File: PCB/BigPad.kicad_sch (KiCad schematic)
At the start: 27 parts, among them SW1 RotaryEncoder_Switch, SW2 RotaryEncoder_Switch

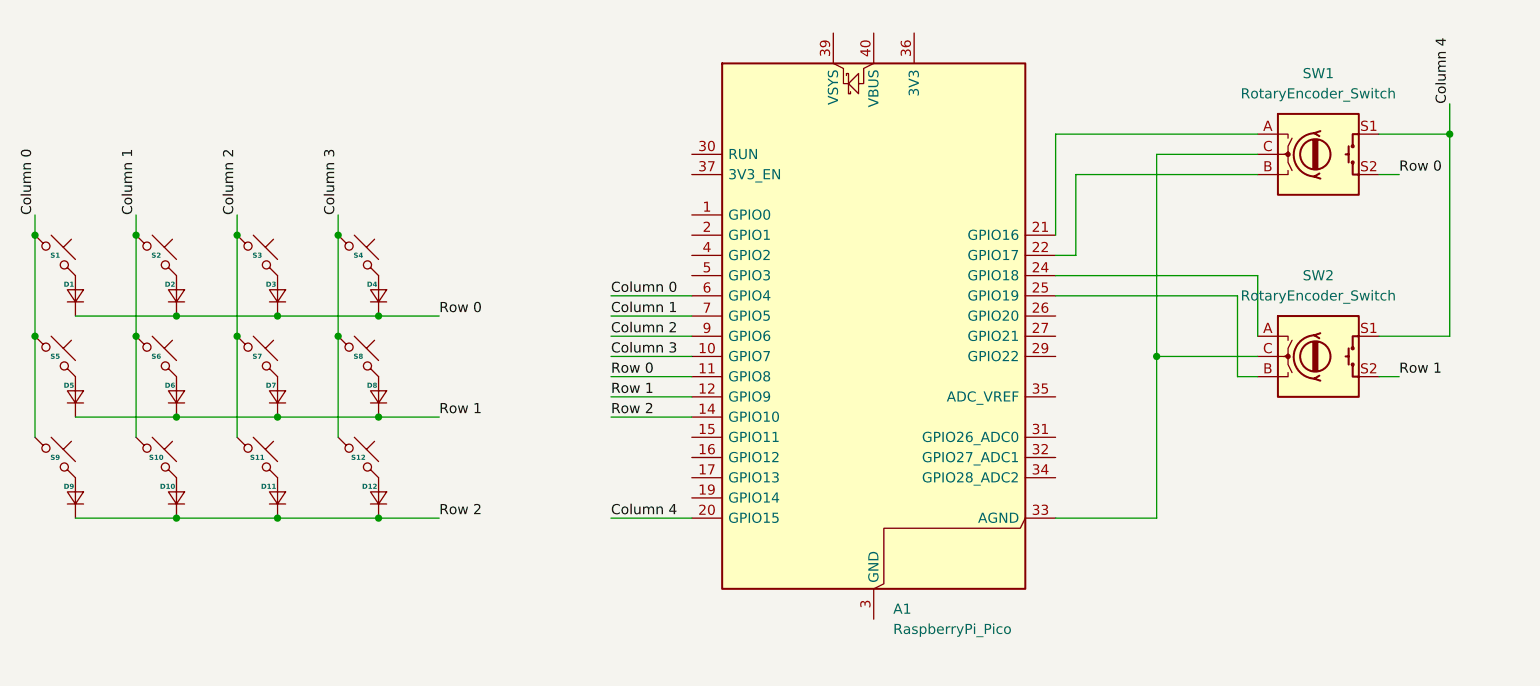
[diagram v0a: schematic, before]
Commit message: Updated rotary encoder wiring in schematic
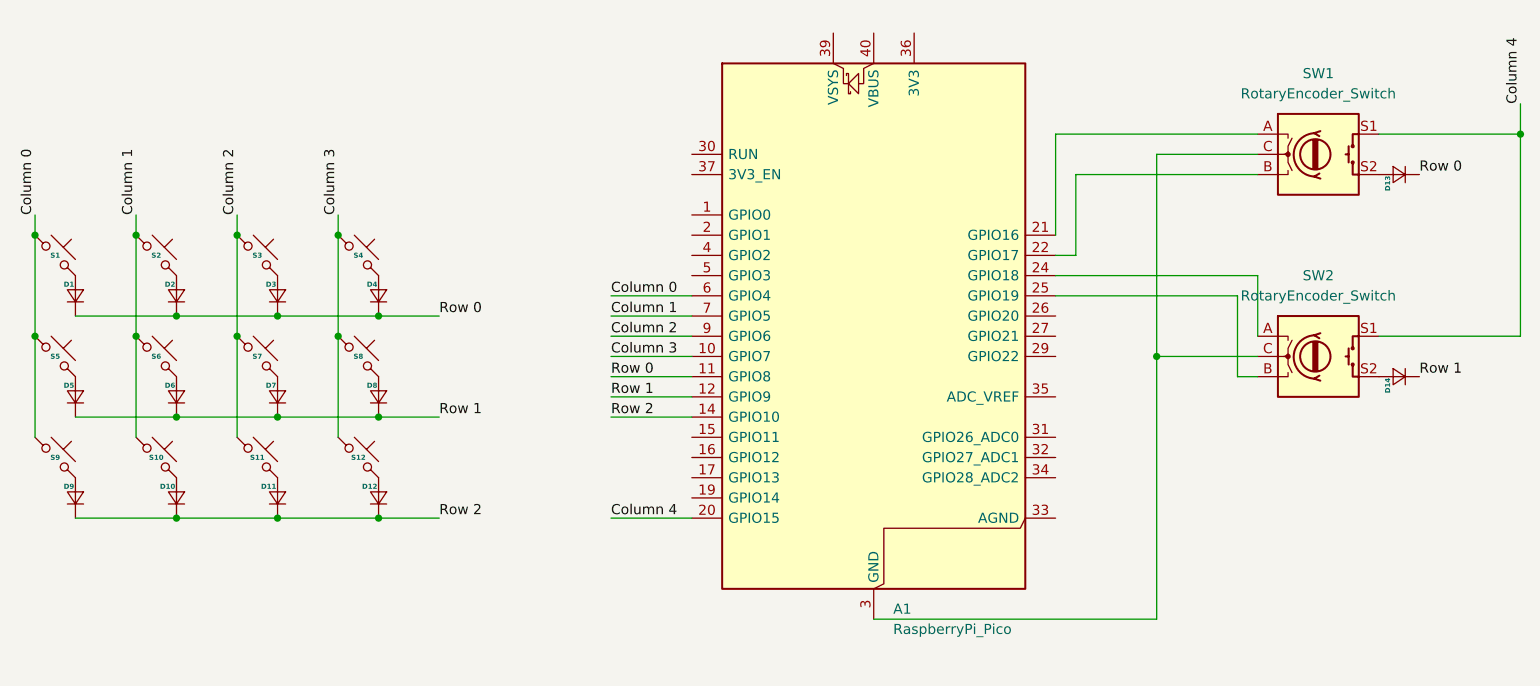
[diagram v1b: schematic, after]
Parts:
- added D13, D14: (no value), ScottoKeebs_Components:Diode_DO-35, symbol ScottoKeebs:Placeholder_Diode
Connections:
- net Row 0: now also D13.1 (K); no longer SW1.S2
- net Row 1: now also D14.1 (K); no longer SW2.S2
- net at SW1.C, SW2.C: now also A1.13 (GND), A1.18 (GND), A1.23 (GND), A1.28 (GND), A1.3 (GND), A1.38 (GND), A1.8 (GND); no longer A1.33 (AGND)
- new net: D14.2 (A), SW2.S2
- new net: D13.2 (A), SW1.S2
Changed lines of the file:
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@@
-	)
-	(junction
-		(at 201.93 54.61)
-		(diameter 0)
-		(color 0 0 0 0)
 	)
 	(junction
@@
 	)
 	(junction
+		(at 210.82 54.61)
+		(diameter 0)
+		(color 0 0 0 0)
+	)
+	(junction
 		(at 67.31 102.87)
 		(diameter 0)
@@
 	(wire
 		(pts
-			(xy 201.93 54.61) (xy 193.04 54.61)
+			(xy 193.04 54.61) (xy 210.82 54.61)
 		)
 		(stroke
@@
 	(wire
 		(pts
-			(xy 152.4 102.87) (xy 165.1 102.87)
-		)
-		(stroke
-			(width 0)
-			(type default)
-		)
-	)
-	(wire
-		(pts
 			(xy 96.52 87.63) (xy 106.68 87.63)
 		)
@@
 	(wire
 		(pts
-			(xy 193.04 80.01) (xy 201.93 80.01)
+			(xy 193.04 80.01) (xy 210.82 80.01)
 		)
 		(stroke
@@
 	(wire
 		(pts
-			(xy 195.58 59.69) (xy 193.04 59.69)
-		)
-		(stroke
-			(width 0)
-			(type default)
-		)
-	)
-	(wire
-		(pts
 			(xy 177.8 57.15) (xy 165.1 57.15)
 		)
@@
 	(wire
 		(pts
-			(xy 165.1 102.87) (xy 165.1 82.55)
-		)
-		(stroke
-			(width 0)
-			(type default)
-		)
-	)
-	(wire
-		(pts
-			(xy 201.93 54.61) (xy 201.93 80.01)
+			(xy 165.1 82.55) (xy 165.1 115.57)
+		)
+		(stroke
+			(width 0)
+			(type default)
+		)
+	)
+	(wire
+		(pts
+			(xy 210.82 54.61) (xy 210.82 80.01)
 		)
 		(stroke
@@
 	(wire
 		(pts
+			(xy 165.1 115.57) (xy 129.54 115.57)
+		)
+		(stroke
+			(width 0)
+			(type default)
+		)
+	)
+	(wire
+		(pts
 			(xy 154.94 59.69) (xy 177.8 59.69)
 		)
@@
 	(wire
 		(pts
-			(xy 195.58 85.09) (xy 193.04 85.09)
-		)
-		(stroke
-			(width 0)
-			(type default)
-		)
-	)
-	(wire
-		(pts
 			(xy 74.93 90.17) (xy 67.31 90.17)
 		)
@@
 	(wire
 		(pts
-			(xy 201.93 50.8) (xy 201.93 54.61)
+			(xy 210.82 50.8) (xy 210.82 54.61)
 		)
 		(stroke
@@
 	)
 	(label "Row 0"
-		(at 195.58 59.69 0)
-		(effects
-			(font
-				(size 1.27 1.27)
-			)
-			(justify left bottom)
-		)
-	)
-	(label "Row 0"
 		(at 74.93 77.47 0)
 		(effects
@@
 	)
 	(label "Column 4"
-		(at 201.93 50.8 90)
+		(at 210.82 50.8 90)
 		(effects
 			(font
@@
 		)
 	)
+	(label "Row 0"
+		(at 198.12 59.69 0)
+		(effects
+			(font
+				(size 1.27 1.27)
+			)
+			(justify left bottom)
+		)
+	)
 	(label "Column 2"
 		(at 49.53 64.77 90)
@@
 		)
 	)
+	(label "Row 1"
+		(at 198.12 85.09 0)
+		(effects
+			(font
+				(size 1.27 1.27)
+			)
+			(justify left bottom)
+		)
+	)
 	(label "Column 1"
 		(at 96.52 77.47 0)
@@
 	(label "Column 4"
 		(at 96.52 102.87 0)
-		(effects
-			(font
-				(size 1.27 1.27)
-			)
-			(justify left bottom)
-		)
-	)
-	(label "Row 1"
-		(at 195.58 85.09 0)
 		(effects
 			(font
@@
 	)
 	(symbol
+		(lib_id "ScottoKeebs:Placeholder_Diode")
+		(at 195.58 85.09 90)
+		(unit 1)
+		(body_style 1)
+		(exclude_from_sim no)
+		(in_bom yes)
+		(on_board yes)
+		(in_pos_files yes)
+		(dnp no)
+		(fields_autoplaced yes)
+		(property "Reference" "D14"
+			(at 194.514 85.24 0)
+			(show_name no)
+			(do_not_autoplace yes)
+			(effects
+				(font
+					(size 0.635 0.635)
+					(thickness 0.127)
+					(bold yes)
+				)
+				(justify right bottom)
+			)
+		)
+		(property "Value" ""
+			(at 195.58 82.55 90)
+			(show_name no)
+			(do_not_autoplace no)
+			(effects
+				(font
+					(size 1.27 1.27)
+				)
+			)
+		)
+		(property "Footprint" "ScottoKeebs_Components:Diode_DO-35"
+			(at 195.58 85.09 90)
+			(hide yes)
+			(show_name no)
+			(do_not_autoplace no)
+			(effects
+				(font
+					(size 1.27 1.27)
+				)
+			)
+		)
+		(property "Datasheet" ""
+			(at 195.58 85.09 90)
+			(hide yes)
+			(show_name no)
+			(do_not_autoplace no)
+			(effects
+				(font
+					(size 1.27 1.27)
+				)
+			)
+		)
+		(property "Description" ""
+			(at 195.58 81.28 90)
+			(hide yes)
+			(show_name no)
+			(do_not_autoplace no)
+			(effects
+				(font
+					(size 1.27 1.27)
+				)
+			)
+		)
+		(pin "1"
+		)
+		(pin "2"
+		)
+		(instances
+			(project "BigPad"
+				(path "/57af516c-98c7-406a-8dd4-07f33deb6b10"
+					(reference "D14")
+					(unit 1)
+				)
+			)
+		)
+	)
+	(symbol
 		(lib_id "ScottoKeebs:Placeholder_Keyswitch")
 		(at 39.37 82.55 0)
@@
 					(unit 1)
 				)
+			)
+		)
+	)
+	(symbol
+		(lib_id "ScottoKeebs:Placeholder_Diode")
+		(at 195.58 59.69 90)
+		(unit 1)
+		(body_style 1)
+		(exclude_from_sim no)
+		(in_bom yes)
+		(on_board yes)
+		(in_pos_files yes)
+		(dnp no)
+		(fields_autoplaced yes)
+		(property "Reference" "D13"
+			(at 194.514 59.84 0)
+			(show_name no)
+			(do_not_autoplace yes)
+			(effects
+				(font
+					(size 0.635 0.635)
+					(thickness 0.127)
+					(bold yes)
+				)
+				(justify right bottom)
+			)
+		)
+		(property "Value" ""
+			(at 195.58 57.15 90)
+			(show_name no)
+			(do_not_autoplace no)
+			(effects
+				(font
+					(size 1.27 1.27)
+				)
+			)
+		)
+		(property "Footprint" "ScottoKeebs_Components:Diode_DO-35"
+			(at 195.58 59.69 90)
+			(hide yes)
+			(show_name no)
+			(do_not_autoplace no)
+			(effects
+				(font
+					(size 1.27 1.27)
+				)
+			)
+		)
+		(property "Datasheet" ""
+			(at 195.58 59.69 90)
+			(hide yes)
+			(show_name no)
+			(do_not_autoplace no)
+			(effects
+				(font
+					(size 1.27 1.27)
+				)
+			)
+		)
+		(property "Description" ""
+			(at 195.58 55.88 90)
+			(hide yes)
+			(show_name no)
+			(do_not_autoplace no)
+			(effects
+				(font
+					(size 1.27 1.27)
+				)
+			)
+		)
+		(pin "1"
+		)
+		(pin "2"
+		)
+		(instances
+			(project "BigPad"
+				(path "/57af516c-98c7-406a-8dd4-07f33deb6b10"
+					(reference "D13")
+					(unit 1)
+				)

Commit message: completed rotary encoders in PCB design
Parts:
- A1: footprint Module:RaspberryPi_Pico_Common_SMD -> Module:RaspberryPi_Pico_Common_THT
- SW1, SW2: footprint (none) -> Rotary_Encoder:RotaryEncoder_Alps_EC11E-Switch_Vertical_H20mm_MountingHoles
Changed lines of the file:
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@@
 			)
 		)
-		(property "Footprint" ""
+		(property "Footprint" "Rotary_Encoder:RotaryEncoder_Alps_EC11E-Switch_Vertical_H20mm_MountingHoles"
 			(at 181.61 53.086 0)
 			(hide yes)
@@
 			)
 		)
-		(property "Footprint" "Module:RaspberryPi_Pico_Common_SMD"
+		(property "Footprint" "Module:RaspberryPi_Pico_Common_THT"
 			(at 129.54 127 0)
 			(hide yes)
@@
 			)
 		)
-		(property "Footprint" ""
+		(property "Footprint" "Rotary_Encoder:RotaryEncoder_Alps_EC11E-Switch_Vertical_H20mm_MountingHoles"
 			(at 181.61 78.486 0)
 			(hide yes)

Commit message: fixed several wiring issues
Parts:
- D1, D10, D11, D12, D13, D14, D2, D3, D4, D5, D6, D7, D8, D9: footprint ScottoKeebs_Components:Diode_DO-35 -> Diode_SMD:D_SOD-123
- S1, S10, S11, S12, S2, S3, S4, S5, S6, S7, S8, S9: footprint ScottoKeebs_MX:MX_PCB_1.00u -> PCM_Switch_Keyboard_Hotswap_Kailh:SW_Hotswap_Kailh_MX_Plated_1.00u
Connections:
- net GND: now reaches A1.13 (GND), A1.18 (GND), A1.23 (GND), A1.28 (GND), A1.3 (GND), A1.38 (GND), A1.8 (GND), SW1.C, SW2.C
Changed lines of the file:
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@@
 	)
 	(junction
-		(at 165.1 82.55)
-		(diameter 0)
-		(color 0 0 0 0)
-	)
-	(junction
 		(at 41.91 102.87)
 		(diameter 0)
@@
 	)
 	(junction
+		(at 165.1 82.55)
+		(diameter 0)
+		(color 0 0 0 0)
+	)
+	(junction
 		(at 67.31 77.47)
 		(diameter 0)
@@
 	(wire
 		(pts
+			(xy 165.1 86.36) (xy 165.1 82.55)
+		)
+		(stroke
+			(width 0)
+			(type default)
+		)
+	)
+	(wire
+		(pts
 			(xy 74.93 77.47) (xy 67.31 77.47)
 		)
@@
 	(wire
 		(pts
-			(xy 165.1 82.55) (xy 165.1 115.57)
-		)
-		(stroke
-			(width 0)
-			(type default)
-		)
-	)
-	(wire
-		(pts
 			(xy 210.82 54.61) (xy 210.82 80.01)
 		)
@@
 	(wire
 		(pts
-			(xy 165.1 115.57) (xy 129.54 115.57)
-		)
-		(stroke
-			(width 0)
-			(type default)
-		)
-	)
-	(wire
-		(pts
 			(xy 154.94 59.69) (xy 177.8 59.69)
 		)
@@
 	)
 	(symbol
+		(lib_id "power:GND")
+		(at 129.54 115.57 0)
+		(unit 1)
+		(body_style 1)
+		(exclude_from_sim no)
+		(in_bom yes)
+		(on_board yes)
+		(in_pos_files yes)
+		(dnp no)
+		(fields_autoplaced yes)
+		(property "Reference" "#PWR01"
+			(at 129.54 121.92 0)
+			(hide yes)
+			(show_name no)
+			(do_not_autoplace no)
+			(effects
+				(font
+					(size 1.27 1.27)
+				)
+			)
+		)
+		(property "Value" "GND"
+			(at 129.54 120.65 0)
+			(show_name no)
+			(do_not_autoplace no)
+			(effects
+				(font
+					(size 1.27 1.27)
+				)
+			)
+		)
+		(property "Footprint" ""
+			(at 129.54 115.57 0)
+			(hide yes)
+			(show_name no)
+			(do_not_autoplace no)
+			(effects
+				(font
+					(size 1.27 1.27)
+				)
+			)
+		)
+		(property "Datasheet" ""
+			(at 129.54 115.57 0)
+			(hide yes)
+			(show_name no)
+			(do_not_autoplace no)
+			(effects
+				(font
+					(size 1.27 1.27)
+				)
+			)
+		)
+		(property "Description" "Power symbol creates a global label with name \"GND\" , ground"
+			(at 129.54 115.57 0)
+			(hide yes)
+			(show_name no)
+			(do_not_autoplace no)
+			(effects
+				(font
+					(size 1.27 1.27)
+				)
+			)
+		)
+		(pin "1"
+		)
+		(instances
+			(project "BigPad"
+				(path "/57af516c-98c7-406a-8dd4-07f33deb6b10"
+					(reference "#PWR01")
+					(unit 1)
+				)
+			)
+		)
+	)
+	(symbol
 		(lib_id "ScottoKeebs:Placeholder_Keyswitch")
 		(at 39.37 69.85 0)
@@
 			)
 		)
-		(property "Footprint" "ScottoKeebs_MX:MX_PCB_1.00u"
+		(property "Footprint" "PCM_Switch_Keyboard_Hotswap_Kailh:SW_Hotswap_Kailh_MX_Plated_1.00u"
 			(at 39.37 69.85 0)
 			(hide yes)
@@
 			)
 		)
-		(property "Footprint" "ScottoKeebs_Components:Diode_DO-35"
+		(property "Footprint" "Diode_SMD:D_SOD-123"
 			(at 195.58 85.09 90)
 			(hide yes)
@@
 			)
 		)
-		(property "Footprint" "ScottoKeebs_MX:MX_PCB_1.00u"
+		(property "Footprint" "PCM_Switch_Keyboard_Hotswap_Kailh:SW_Hotswap_Kailh_MX_Plated_1.00u"
 			(at 39.37 82.55 0)
 			(hide yes)
@@
 			)
 		)
-		(property "Footprint" "ScottoKeebs_Components:Diode_DO-35"
+		(property "Footprint" "Diode_SMD:D_SOD-123"
 			(at 54.61 87.63 90)
 			(hide yes)
@@
 			)
 		)
-		(property "Footprint" "ScottoKeebs_Components:Diode_DO-35"
+		(property "Footprint" "Diode_SMD:D_SOD-123"
 			(at 195.58 59.69 90)
 			(hide yes)
@@
 			)
 		)
-		(property "Footprint" "ScottoKeebs_Components:Diode_DO-35"
+		(property "Footprint" "Diode_SMD:D_SOD-123"
 			(at 29.21 87.63 90)
 			(hide yes)
@@
 			)
 		)
-		(property "Footprint" "ScottoKeebs_Components:Diode_DO-35"
+		(property "Footprint" "Diode_SMD:D_SOD-123"
 			(at 67.31 100.33 90)
 			(hide yes)
@@
 			)
 		)
-		(property "Footprint" "ScottoKeebs_Components:Diode_DO-35"
+		(property "Footprint" "Diode_SMD:D_SOD-123"
 			(at 67.31 87.63 90)
 			(hide yes)
@@
 			)
 		)
-		(property "Footprint" "ScottoKeebs_Components:Diode_DO-35"
+		(property "Footprint" "Diode_SMD:D_SOD-123"
 			(at 67.31 74.93 90)
 			(hide yes)
@@
 			)
 		)
-		(property "Footprint" "ScottoKeebs_Components:Diode_DO-35"
+		(property "Footprint" "Diode_SMD:D_SOD-123"
 			(at 29.21 74.93 90)
 			(hide yes)
@@
 	)
 	(symbol
+		(lib_id "power:GND")
+		(at 165.1 86.36 0)
+		(unit 1)
+		(body_style 1)
+		(exclude_from_sim no)
+		(in_bom yes)
+		(on_board yes)
+		(in_pos_files yes)
+		(dnp no)
+		(fields_autoplaced yes)
+		(property "Reference" "#PWR02"
+			(at 165.1 92.71 0)
+			(hide yes)
+			(show_name no)
+			(do_not_autoplace no)
+			(effects
+				(font
+					(size 1.27 1.27)
+				)
+			)
+		)
+		(property "Value" "GND"
+			(at 165.1 91.44 0)
+			(show_name no)
+			(do_not_autoplace no)
+			(effects
+				(font
+					(size 1.27 1.27)
+				)
+			)
+		)
+		(property "Footprint" ""
+			(at 165.1 86.36 0)
+			(hide yes)
+			(show_name no)
+			(do_not_autoplace no)
+			(effects
+				(font
+					(size 1.27 1.27)
+				)
+			)
+		)
+		(property "Datasheet" ""
+			(at 165.1 86.36 0)
+			(hide yes)
+			(show_name no)
+			(do_not_autoplace no)
+			(effects
+				(font
+					(size 1.27 1.27)
+				)
+			)
+		)
+		(property "Description" "Power symbol creates a global label with name \"GND\" , ground"
+			(at 165.1 86.36 0)
+			(hide yes)
+			(show_name no)
+			(do_not_autoplace no)
+			(effects
+				(font
+					(size 1.27 1.27)
+				)
+			)
+		)
+		(pin "1"
+		)
+		(instances
+			(project "BigPad"
+				(path "/57af516c-98c7-406a-8dd4-07f33deb6b10"
+					(reference "#PWR02")
+					(unit 1)
+				)
+			)
+		)
+	)
+	(symbol
 		(lib_id "ScottoKeebs:Placeholder_Keyswitch")
 		(at 64.77 82.55 0)
@@
 			)
 		)
-		(property "Footprint" "ScottoKeebs_MX:MX_PCB_1.00u"
+		(property "Footprint" "PCM_Switch_Keyboard_Hotswap_Kailh:SW_Hotswap_Kailh_MX_Plated_1.00u"
 			(at 64.77 82.55 0)
 			(hide yes)
@@
 			)
 		)
-		(property "Footprint" "ScottoKeebs_Components:Diode_DO-35"
+		(property "Footprint" "Diode_SMD:D_SOD-123"
 			(at 41.91 74.93 90)
 			(hide yes)
@@
 			)
 		)
-		(property "Footprint" "ScottoKeebs_MX:MX_PCB_1.00u"
+		(property "Footprint" "PCM_Switch_Keyboard_Hotswap_Kailh:SW_Hotswap_Kailh_MX_Plated_1.00u"
 			(at 26.67 82.55 0)
 			(hide yes)
@@
 			)
 		)
-		(property "Footprint" "ScottoKeebs_MX:MX_PCB_1.00u"
+		(property "Footprint" "PCM_Switch_Keyboard_Hotswap_Kailh:SW_Hotswap_Kailh_MX_Plated_1.00u"
 			(at 52.07 95.25 0)
 			(hide yes)
@@
 			)
 		)
-		(property "Footprint" "ScottoKeebs_MX:MX_PCB_1.00u"
+		(property "Footprint" "PCM_Switch_Keyboard_Hotswap_Kailh:SW_Hotswap_Kailh_MX_Plated_1.00u"
 			(at 64.77 69.85 0)
 			(hide yes)
@@
 			)
 		)
-		(property "Footprint" "ScottoKeebs_MX:MX_PCB_1.00u"
+		(property "Footprint" "PCM_Switch_Keyboard_Hotswap_Kailh:SW_Hotswap_Kailh_MX_Plated_1.00u"
 			(at 52.07 82.55 0)
 			(hide yes)
@@
 			)
 		)
-		(property "Footprint" "ScottoKeebs_Components:Diode_DO-35"
+		(property "Footprint" "Diode_SMD:D_SOD-123"
 			(at 41.91 100.33 90)
 			(hide yes)
@@
 			)
 		)
-		(property "Footprint" "ScottoKeebs_Components:Diode_DO-35"
+		(property "Footprint" "Diode_SMD:D_SOD-123"
 			(at 54.61 100.33 90)
 			(hide yes)
@@
 			)
 		)
-		(property "Footprint" "ScottoKeebs_Components:Diode_DO-35"
+		(property "Footprint" "Diode_SMD:D_SOD-123"
 			(at 54.61 74.93 90)
 			(hide yes)
@@
 			)
 		)
-		(property "Footprint" "ScottoKeebs_MX:MX_PCB_1.00u"
+		(property "Footprint" "PCM_Switch_Keyboard_Hotswap_Kailh:SW_Hotswap_Kailh_MX_Plated_1.00u"
 			(at 26.67 69.85 0)
 			(hide yes)
@@
 			)
 		)
-		(property "Footprint" "ScottoKeebs_MX:MX_PCB_1.00u"
+		(property "Footprint" "PCM_Switch_Keyboard_Hotswap_Kailh:SW_Hotswap_Kailh_MX_Plated_1.00u"
 			(at 39.37 95.25 0)
 			(hide yes)
@@
 			)
 		)
-		(property "Footprint" "ScottoKeebs_MX:MX_PCB_1.00u"
+		(property "Footprint" "PCM_Switch_Keyboard_Hotswap_Kailh:SW_Hotswap_Kailh_MX_Plated_1.00u"
 			(at 26.67 95.25 0)
 			(hide yes)
@@
 			)
 		)
-		(property "Footprint" "ScottoKeebs_MX:MX_PCB_1.00u"
+		(property "Footprint" "PCM_Switch_Keyboard_Hotswap_Kailh:SW_Hotswap_Kailh_MX_Plated_1.00u"
 			(at 52.07 69.85 0)
 			(hide yes)
@@
 			)
 		)
-		(property "Footprint" "ScottoKeebs_MX:MX_PCB_1.00u"
+		(property "Footprint" "PCM_Switch_Keyboard_Hotswap_Kailh:SW_Hotswap_Kailh_MX_Plated_1.00u"
 			(at 64.77 95.25 0)
 			(hide yes)
@@
 			)
 		)
-		(property "Footprint" "ScottoKeebs_Components:Diode_DO-35"
+		(property "Footprint" "Diode_SMD:D_SOD-123"
 			(at 29.21 100.33 90)
 			(hide yes)
@@
 			)
 		)
-		(property "Footprint" "ScottoKeebs_Components:Diode_DO-35"
+		(property "Footprint" "Diode_SMD:D_SOD-123"
 			(at 41.91 87.63 90)
 			(hide yes)
